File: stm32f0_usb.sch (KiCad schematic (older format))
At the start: 32 parts, among them J1 USB_B_Mini, J2 Conn_ARM_JTAG_SWD_10, J3 Conn_01x14_Male, J4 Conn_01x14_Male, SW1 B3S-1000P, SW2 B3S-1000P, U2 ADP121-AUJZ33R7, U3 USBLC6-2SC6

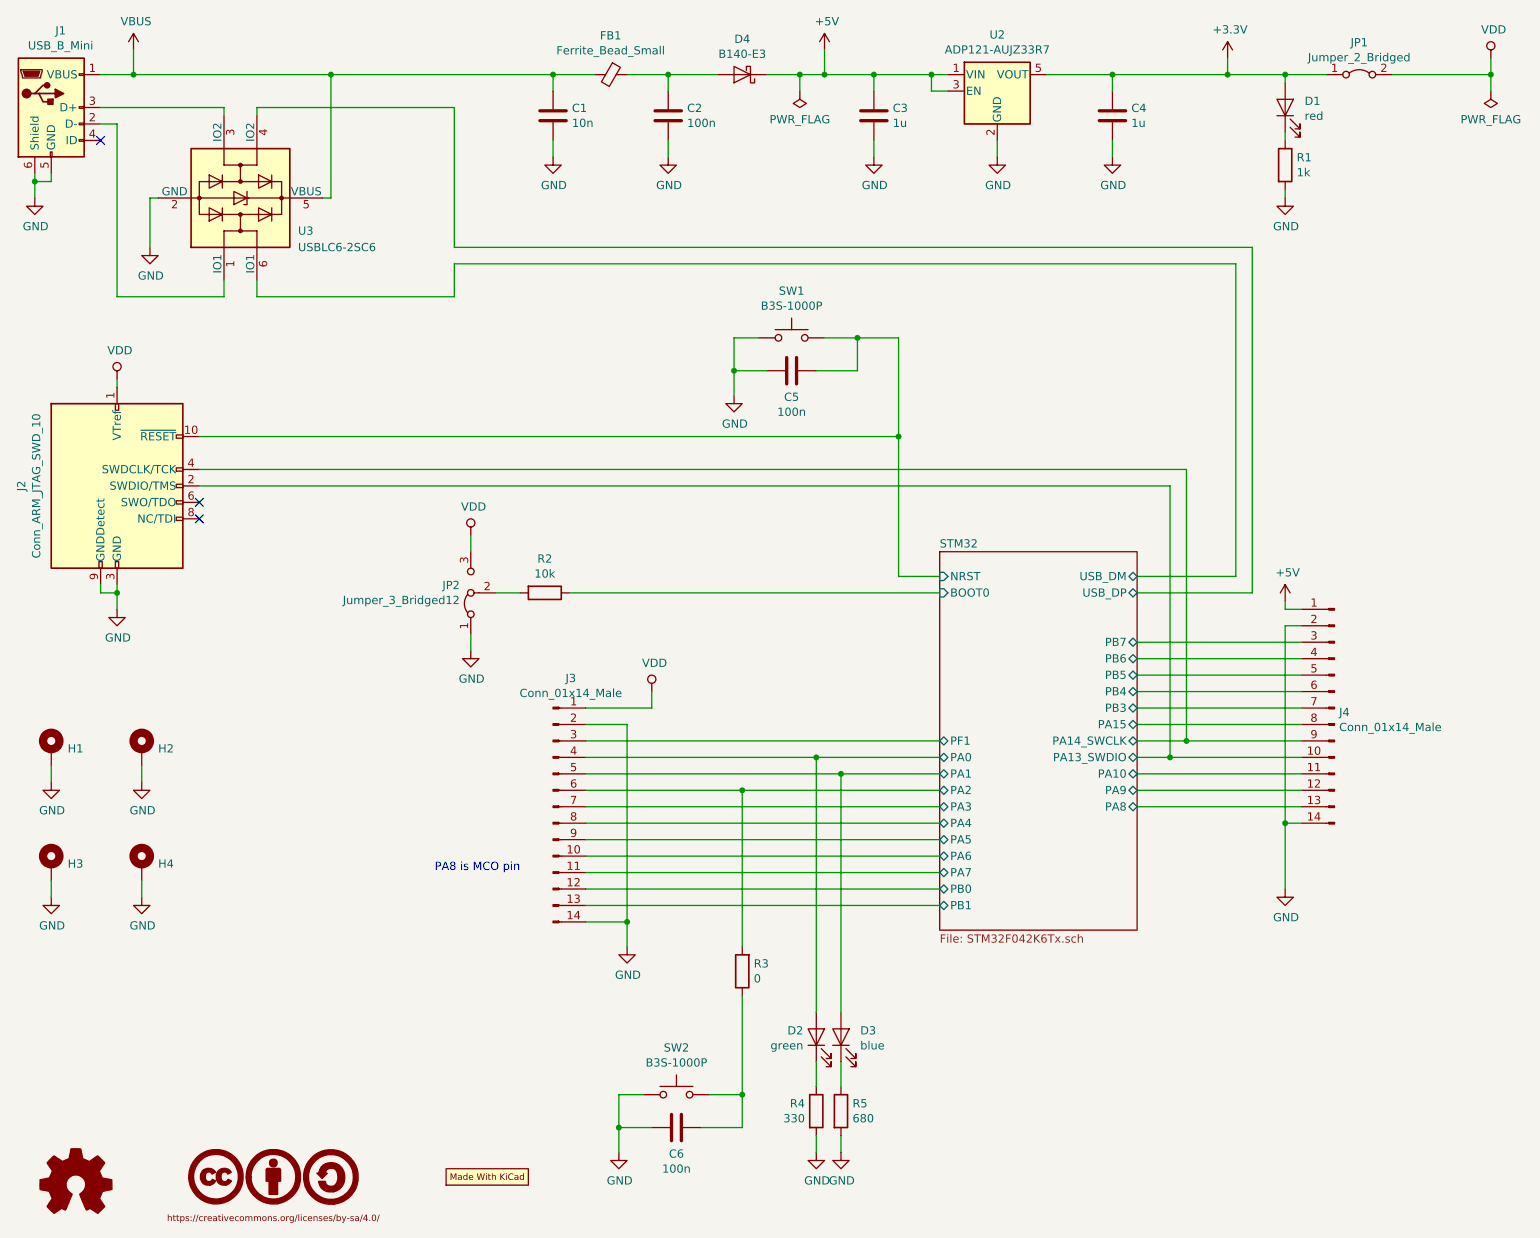
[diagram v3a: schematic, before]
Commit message: complete routing
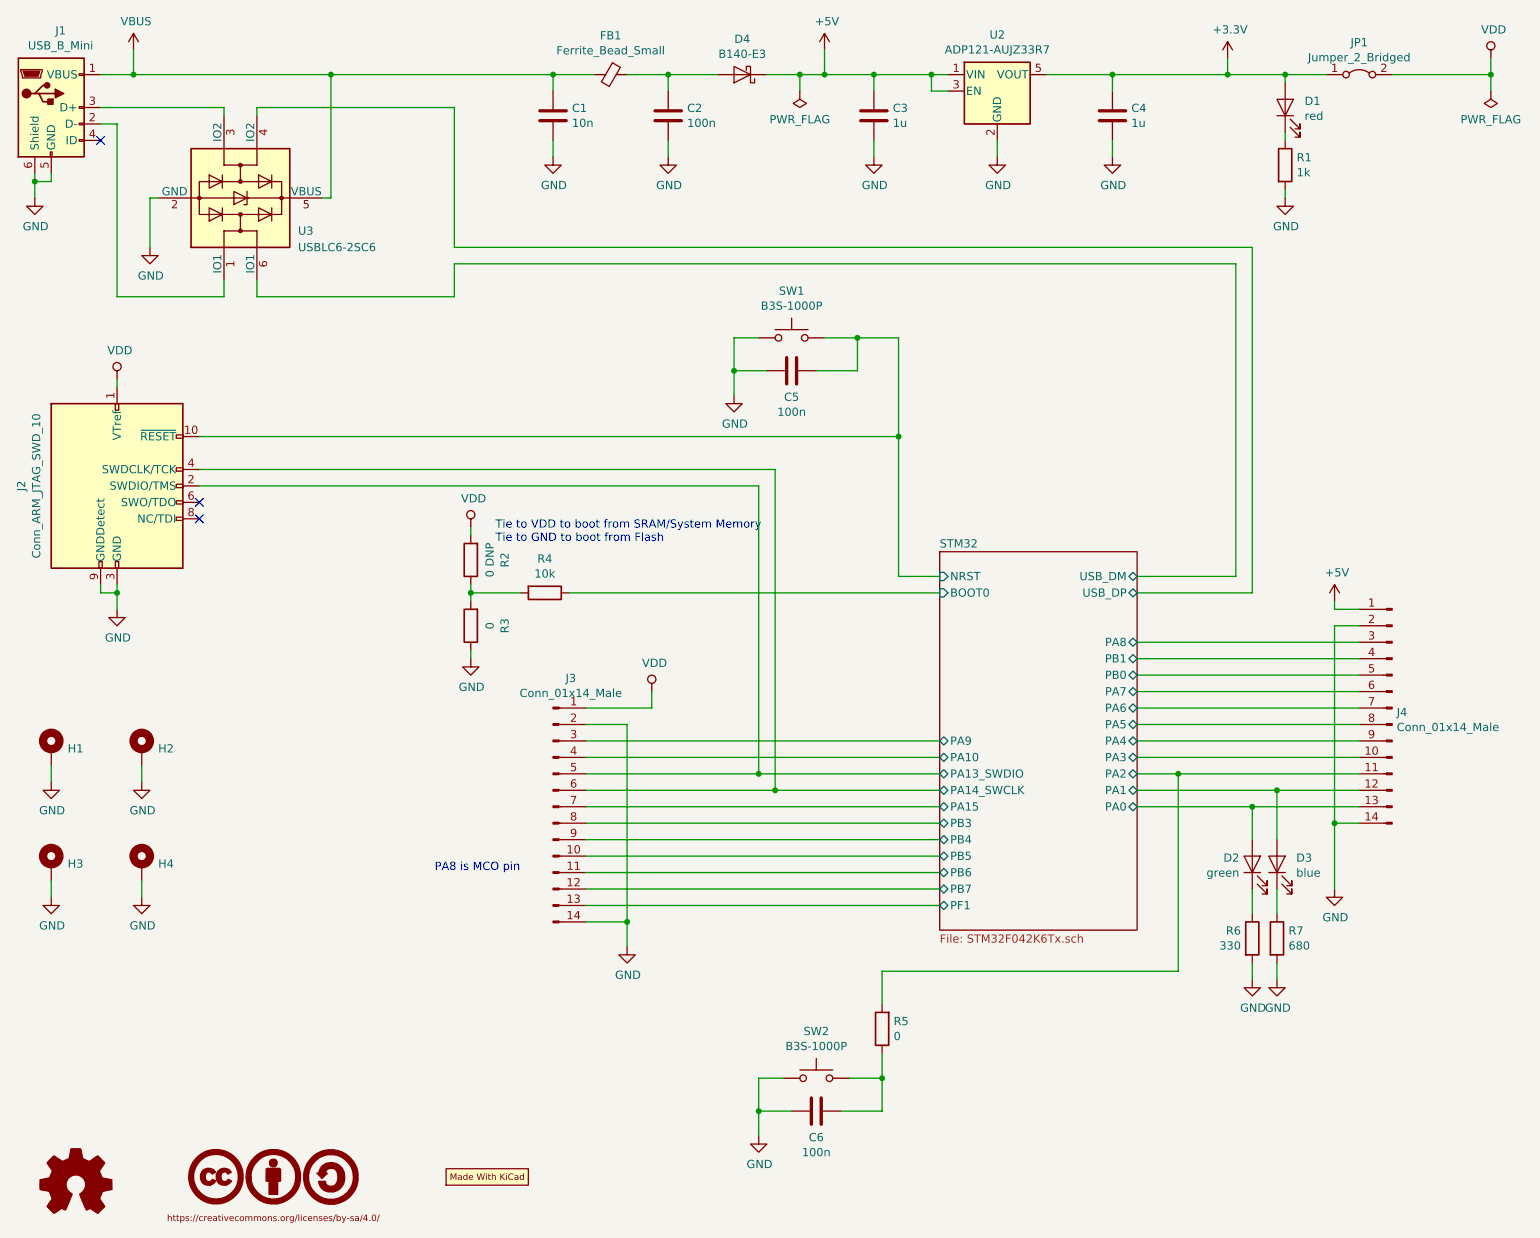
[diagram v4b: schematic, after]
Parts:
- removed JP2: Jumper_3_Bridged12, Connector_PinHeader_2.54mm:PinHeader_1x03_P2.54mm_Vertical, symbol Jumper:Jumper_3_Bridged12
- added LOGO3: Logo_Open_Hardware_Small, Symbol:OSHW-Symbol_6.7x6mm_SilkScreen, symbol Graphic:Logo_Open_Hardware_Small
- added R2: 0 DNP, Resistor_SMD:R_0603_1608Metric, symbol Device:R
- added R3: 0, Resistor_SMD:R_0603_1608Metric, symbol Device:R
- renumbered R2 to R4, R3 to R5, R4 to R6, R5 to R7
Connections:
- net GND: now also R3.1
- net STM32/PA0: now also J4.13 (Pin_13); no longer J3.4 (Pin_4)
- net STM32/PA1: now also J4.12 (Pin_12); no longer J3.5 (Pin_5)
- net STM32/PA10: now also J3.4 (Pin_4); no longer J4.11 (Pin_11)
- net STM32/PA13_SWDIO: now also J3.5 (Pin_5); no longer J4.10 (Pin_10)
- net STM32/PA14_SWCLK: now also J3.6 (Pin_6); no longer J4.9 (Pin_9)
- net STM32/PA15: now also J3.7 (Pin_7); no longer J4.8 (Pin_8)
- net STM32/PA2: now also J4.11 (Pin_11); no longer J3.6 (Pin_6)
- net STM32/PA3: now also J4.10 (Pin_10); no longer J3.7 (Pin_7)
- net STM32/PA4: now also J4.9 (Pin_9); no longer J3.8 (Pin_8)
- net STM32/PA5: now also J4.8 (Pin_8); no longer J3.9 (Pin_9)
- net STM32/PA6: now also J4.7 (Pin_7); no longer J3.10 (Pin_10)
- net STM32/PA7: now also J4.6 (Pin_6); no longer J3.11 (Pin_11)
- net STM32/PA8: now also J4.3 (Pin_3); no longer J4.13 (Pin_13)
- net STM32/PA9: now also J3.3 (Pin_3); no longer J4.12 (Pin_12)
- net STM32/PB0: now also J4.5 (Pin_5); no longer J3.12 (Pin_12)
- net STM32/PB1: now also J4.4 (Pin_4); no longer J3.13 (Pin_13)
- net STM32/PB3: now also J3.8 (Pin_8); no longer J4.7 (Pin_7)
- net STM32/PB4: now also J3.9 (Pin_9); no longer J4.6 (Pin_6)
- net STM32/PB5: now also J3.10 (Pin_10); no longer J4.5 (Pin_5)
- net STM32/PB6: now also J3.11 (Pin_11); no longer J4.4 (Pin_4)
- net STM32/PB7: now also J3.12 (Pin_12); no longer J4.3 (Pin_3)
- net STM32/PF1: now also J3.13 (Pin_13); no longer J3.3 (Pin_3)
- net VDD: now also R2.2
- net at R4.2: now also R2.1, R3.2
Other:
- note added: "Tie to VDD to boot from SRAM/System Memory\nTie to GND to boot from Flash"
- moved on the sheet: C6, D2, D3, J4, R5, R6, R7, SW2
